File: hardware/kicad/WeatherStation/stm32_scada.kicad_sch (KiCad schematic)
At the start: 20 parts, among them J16 RS485 Bus (Phoenix MC), J17 ESP32-S3 Bridge (Header), SW3 MODE_SELECT, U10 STM32F407VGT6, U11 MAX3485ESA+, Y1 8MHz

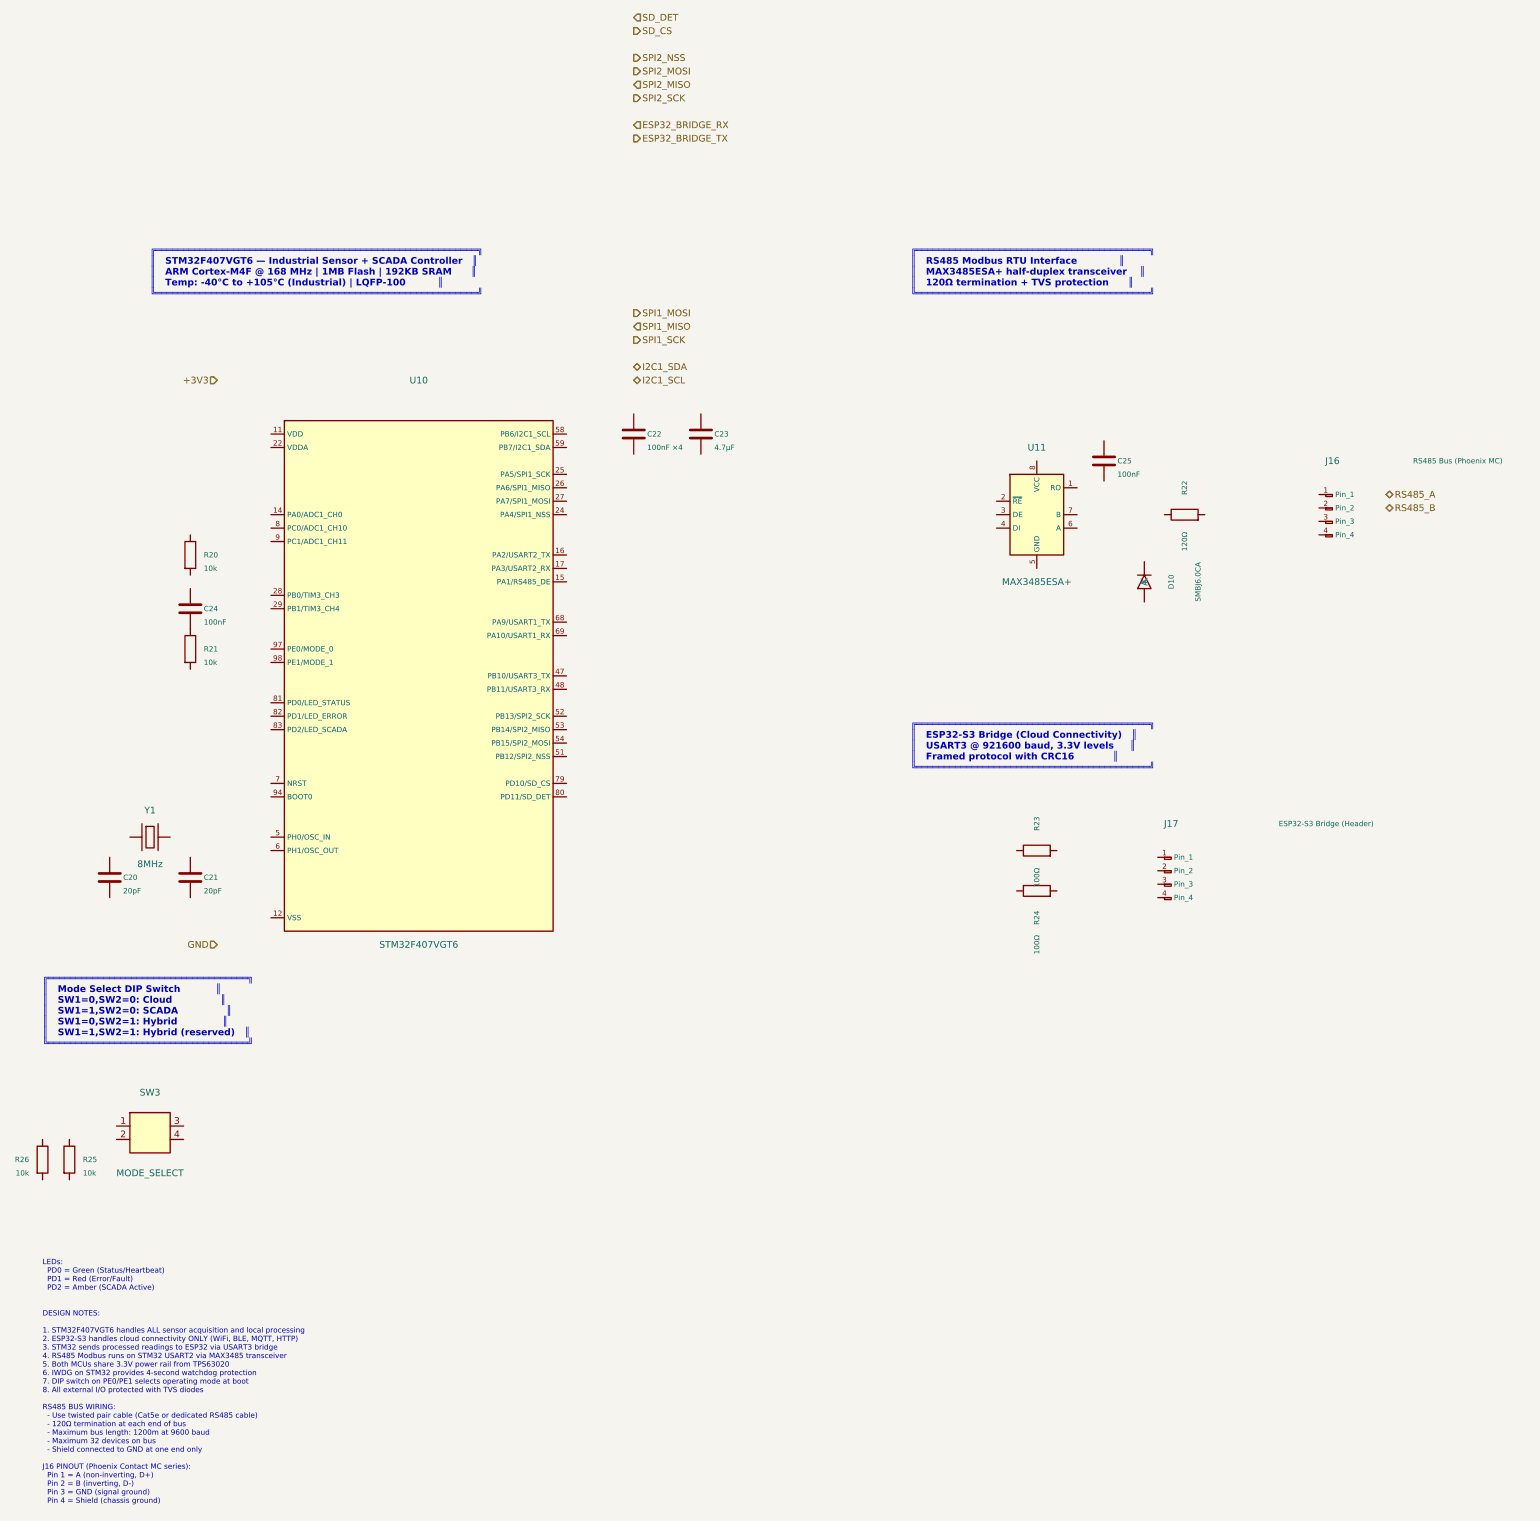
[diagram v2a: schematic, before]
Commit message: Fix 3: stm32_scada.kicad_sch — remove ESP32 bridge J17/R23/R24, remove ESP32_BRIDGE labels, update DESIGN NOTES
Agent-Logs-Url: https://github.com/ppusapati/weather/sessions/bf78e071-0670-4802-a032-1f4282b37237

Co-authored-by: ppusapati <5749576+ppusapati@users.noreply.github.com>
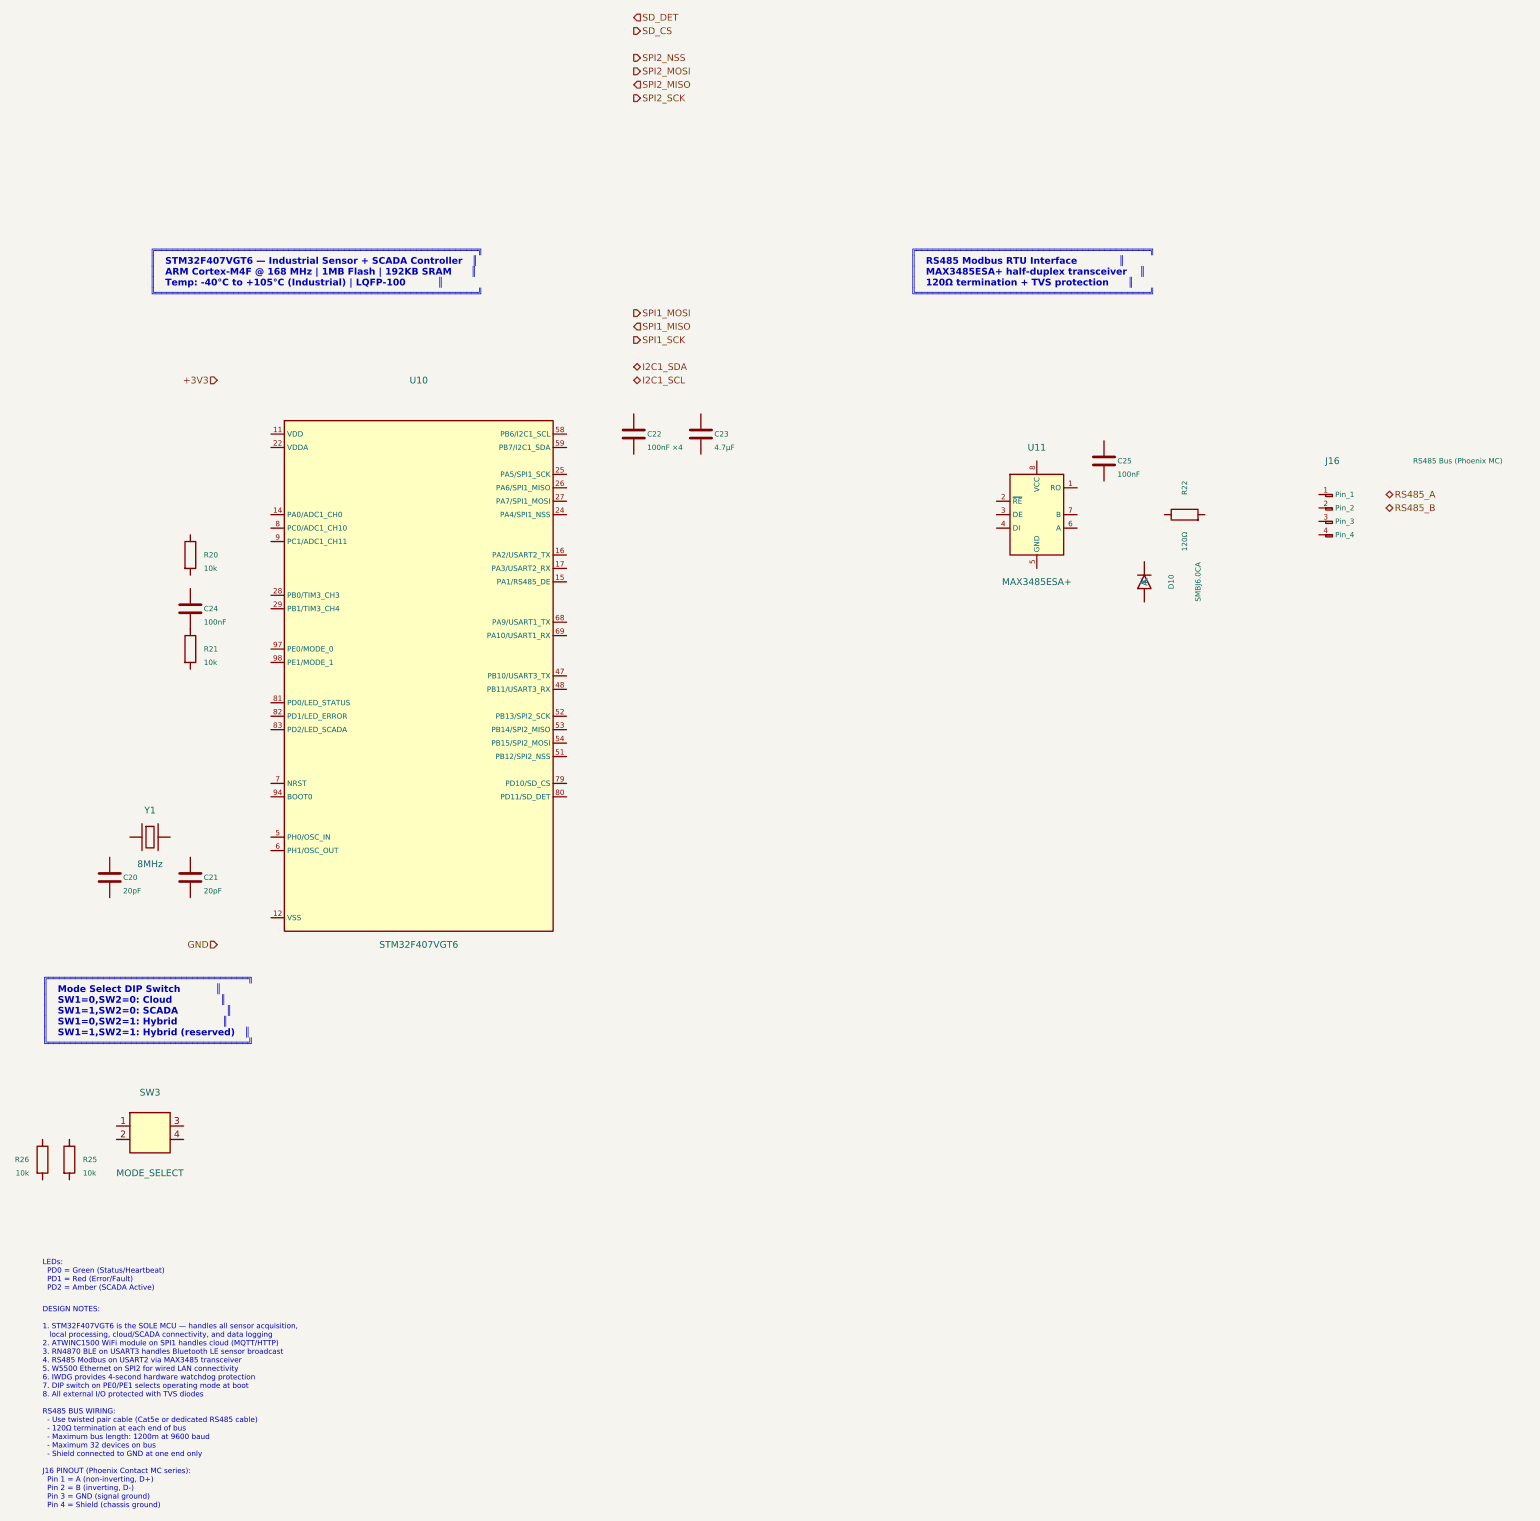
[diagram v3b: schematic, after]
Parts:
- removed J17: ESP32-S3 Bridge (Header), symbol Connector:Conn_01x04
- removed R23, R24: 100Ω, symbol Device:R
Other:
- note added: "DESIGN NOTES: 1. STM32F407VGT6 is the SOLE MCU — handles all sensor acquisition, local processing, cloud/SCADA connectivity, and data logging 2. ATWINC1500 WiFi module on SPI1 handles cloud (MQTT/HTTP) 3. RN4870 BLE on USART3 handles Bluetooth LE sensor broadcast 4. RS485 Modbus on USART2 via MAX3485 transceiver 5. W5500 Ethernet on SPI2 for wired LAN connectivity 6. IWDG provides 4-second hardwa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"
- note removed: "DESIGN NOTES: 1. STM32F407VGT6 handles ALL sensor acquisition and local processing 2. ESP32-S3 handles cloud connectivity ONLY (WiFi, BLE, MQTT, HTTP) 3. STM32 sends processed readings to ESP32 via USART3 bridge 4. RS485 Modbus runs on STM32 USART2 via MAX3485 transceiver 5. Both MCUs share 3.3V power rail from TPS63020 6. IWDG on STM32 provides 4-second watchdog protection 7. DIP switch on PE0/P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"
- note removed: "╔══════════════════════════════════════════╗ ║ ESP32-S3 Bridge (Cloud Connectivity) ║ ║ USART3 @ 921600 baud, 3.3V levels ║ ║ Framed protocol with CRC16 ║ ╚══════════════════════════════════════════╝"
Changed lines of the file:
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@@
     (property "Value" "RS485 Bus (Phoenix MC)" (at 314.96 60.96 0) (effects (font (size 1.0 1.0)) (justify left)))
-  )
-  (text "╔══════════════════════════════════════════╗\n║   ESP32-S3 Bridge (Cloud Connectivity)   ║\n║   USART3 @ 921600 baud, 3.3V levels     ║\n║   Framed protocol with CRC16            ║\n╚══════════════════════════════════════════╝"
-    (at 220 115 0) (effects (font (size 1.27 1.27) (bold yes)) (justify left))
-  )
-  (symbol (lib_id "Connector:Conn_01x04") (at 269.24 139.7 0) (unit 1)
-    (in_bom yes) (on_board yes) (dnp no)
-    (property "Reference" "J17" (at 269.24 129.54 0) (effects (font (size 1.27 1.27))))
-    (property "Value" "ESP32-S3 Bridge (Header)" (at 289.56 129.54 0) (effects (font (size 1.0 1.0)) (justify left)))
-  )
-  (symbol (lib_id "Device:R") (at 243.84 134.62 90) (unit 1)
-    (in_bom yes) (on_board yes) (dnp no)
-    (property "Reference" "R23" (at 243.84 129.54 0) (effects (font (size 1.0 1.0))))
-    (property "Value" "100Ω" (at 243.84 139.7 0) (effects (font (size 1.0 1.0))))
-  )
-  (symbol (lib_id "Device:R") (at 243.84 142.24 90) (unit 1)
-    (in_bom yes) (on_board yes) (dnp no)
-    (property "Reference" "R24" (at 243.84 147.32 0) (effects (font (size 1.0 1.0))))
-    (property "Value" "100Ω" (at 243.84 152.4 0) (effects (font (size 1.0 1.0))))
   )
   (text "╔════════════════════════════════════╗\n║   Mode Select DIP Switch           ║\n║   SW1=0,SW2=0: Cloud               ║\n║   SW1=1,SW2=0: SCADA               ║\n║   SW1=0,SW2=1: Hybrid              ║\n║   SW1=1,SW2=1: Hybrid (reserved)   ║\n╚════════════════════════════════════╝"
@@
     (at 55.88 215 0) (effects (font (size 1.0 1.0)) (justify left))
   )
-  (text "DESIGN NOTES:\n\n1. STM32F407VGT6 handles ALL sensor acquisition and local processing\n2. ESP32-S3 handles cloud connectivity ONLY (WiFi, BLE, MQTT, HTTP)\n3. STM32 sends processed readings to ESP32 via USART3 bridge\n4. RS485 Modbus runs on STM32 USART2 via MAX3485 transceiver\n5. Both MCUs share 3.3V power rail from TPS63020\n6. IWDG on STM32 provides 4-second watchdog protection\n7. DIP switch on PE0/PE1 selects operating mode at boot\n8. All external I/O protected with TVS diodes\n\nRS485 BUS WIRING:\n  - Use twisted pair cable (Cat5e or dedicated RS485 cable)\n  - 120Ω termination at each end of bus\n  - Maximum bus length: 1200m at 9600 baud\n  - Maximum 32 devices on bus\n  - Shield connected to GND at one end only\n\nJ16 PINOUT (Phoenix Contact MC series):\n  Pin 1 = A (non-inverting, D+)\n  Pin 2 = B (inverting, D-)\n  Pin 3 = GND (signal ground)\n  Pin 4 = Shield (chassis ground)"
+  (text "DESIGN NOTES:\n\n1. STM32F407VGT6 is the SOLE MCU — handles all sensor acquisition,\n   local processing, cloud/SCADA connectivity, and data logging\n2. ATWINC1500 WiFi module on SPI1 handles cloud (MQTT/HTTP)\n3. RN4870 BLE on USART3 handles Bluetooth LE sensor broadcast\n4. RS485 Modbus on USART2 via MAX3485 transceiver\n5. W5500 Ethernet on SPI2 for wired LAN connectivity\n6. IWDG provides 4-second hardware watchdog protection\n7. DIP switch on PE0/PE1 selects operating mode at boot\n8. All external I/O protected with TVS diodes\n\nRS485 BUS WIRING:\n  - Use twisted pair cable (Cat5e or dedicated RS485 cable)\n  - 120Ω termination at each end of bus\n  - Maximum bus length: 1200m at 9600 baud\n  - Maximum 32 devices on bus\n  - Shield connected to GND at one end only\n\nJ16 PINOUT (Phoenix Contact MC series):\n  Pin 1 = A (non-inverting, D+)\n  Pin 2 = B (inverting, D-)\n  Pin 3 = GND (signal ground)\n  Pin 4 = Shield (chassis ground)"
     (at 55.88 240 0) (effects (font (size 1.0 1.0)) (justify left))
   )
@@
   (hierarchical_label "GND" (shape input) (at 88.9 152.4 180) (effects (font (size 1.27 1.27)) (justify right))
   )
-  (hierarchical_label "ESP32_BRIDGE_TX" (shape output) (at 167.64 0 0) (effects (font (size 1.27 1.27)) (justify left))
-  )
-  (hierarchical_label "ESP32_BRIDGE_RX" (shape input) (at 167.64 -2.54 0) (effects (font (size 1.27 1.27)) (justify left))
-  )
 )
